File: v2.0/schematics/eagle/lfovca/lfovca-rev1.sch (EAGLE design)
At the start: 35 parts, among them IC1 TL084P, IC2 LM13700N, Q1 2N3906

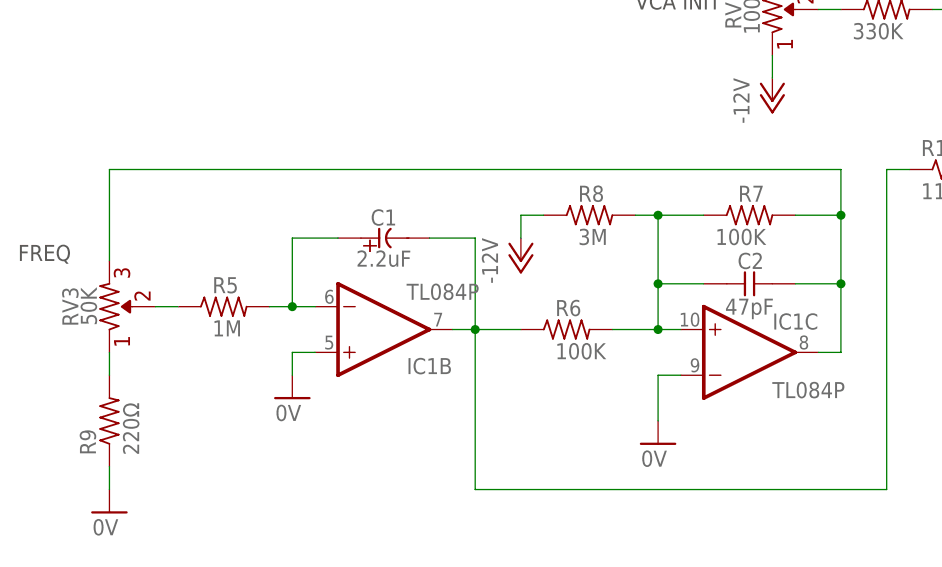
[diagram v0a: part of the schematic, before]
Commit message: Updated values for LFOVCA
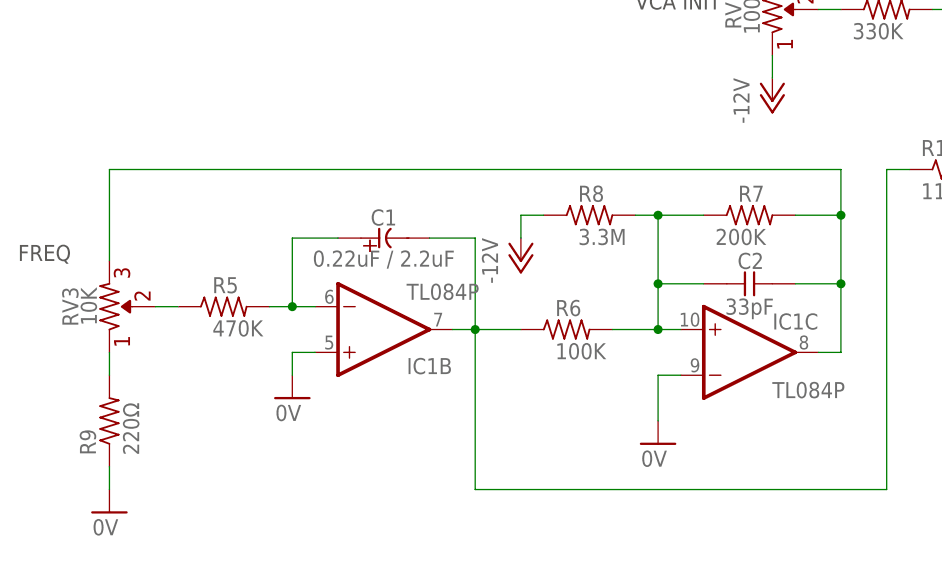
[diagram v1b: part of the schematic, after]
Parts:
- C1: value 2.2uF -> 0.22uF / 2.2uF
- C2: value 47pF -> 33pF
- R5: value 1M -> 470K
- R7: value 100K -> 200K
- R8: value 3M -> 3.3M
- RV3: value 50K -> 10K
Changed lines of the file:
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@@
 <part name="R4" library="resistor" deviceset="R-US_" device="0207/7" value="11K"/>
 <part name="GND4" library="supply1" library_urn="urn:adsk.eagle:library:371" deviceset="0V" device=""/>
-<part name="C1" library="_common.v1" deviceset="CE-US" device="E2-5" value="2.2uF"/>
-<part name="R5" library="resistor" deviceset="R-US_" device="0207/7" value="1M"/>
+<part name="C1" library="_common.v1" deviceset="CE-US" device="E2-5" value="0.22uF / 2.2uF"/>
+<part name="R5" library="resistor" deviceset="R-US_" device="0207/7" value="470K"/>
 <part name="GND5" library="supply1" library_urn="urn:adsk.eagle:library:371" deviceset="0V" device=""/>
 <part name="GND6" library="supply1" library_urn="urn:adsk.eagle:library:371" deviceset="0V" device=""/>
 <part name="R6" library="resistor" deviceset="R-US_" device="0207/7" value="100K"/>
-<part name="R7" library="resistor" deviceset="R-US_" device="0207/7" value="100K"/>
-<part name="R8" library="resistor" deviceset="R-US_" device="0207/7" value="3M"/>
+<part name="R7" library="resistor" deviceset="R-US_" device="0207/7" value="200K"/>
+<part name="R8" library="resistor" deviceset="R-US_" device="0207/7" value="3.3M"/>
 <part name="R9" library="resistor" deviceset="R-US_" device="0207/7" value="220Ω"/>
-<part name="RV3" library="_common" deviceset="R-VAR" device="" value="50K"/>
-<part name="C2" library="_common.v1" deviceset="CC-US" device="025-024X044" value="47pF"/>
+<part name="RV3" library="_common" deviceset="R-VAR" device="" value="10K"/>
+<part name="C2" library="_common.v1" deviceset="CC-US" device="025-024X044" value="33pF"/>
 <part name="GND7" library="supply1" library_urn="urn:adsk.eagle:library:371" deviceset="0V" device=""/>
 <part name="R10" library="resistor" deviceset="R-US_" device="0207/7" value="22Ω"/>
